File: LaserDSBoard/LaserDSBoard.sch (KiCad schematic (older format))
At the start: 181 parts, among them J1 JTAG, J10 Y LIMIT2, J11 LASER, J12 Y VREF, J13 X VREF, J14 Y1 MOTOR, J15 X MOTOR, J16 Y2 MOTOR, J2 USB, J3 POWER IN, J4 LASER P, J5 D SWITCH, J6 WATER FLOW, J7 X LIMIT1, J8 X LIMIT2, J9 Y LIMIT1, SW1 SW_PUSH, SW2 SWITCH_INV, U1 LD1117S33TR, U10 74HC08A, U11 ADUM1250, U12 TLP2355, U13 TLP2355, U14 TLP2355, U15 TLP2355, U16 TLP2355, U17 TLP2355, U18 74HC1G00, U19 MCP3425, U2 LD1117S33TR, U20 A4982SLPTR, U21 A4982SLPTR, U22 TLP2355, U3 STM32F20XR, U4 LD1117S50TR, U5 ADUM1250, U6 TLP627-4, U7 TLP627, U8 MCP44X1, U9 TLP627, X1 CRYSTAL_4PIN, X2 CRYSTAL

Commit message: DSコントロール基板改版
・2→4層化
・Y軸モータードライバ増設(1→2)
・コネクタ変更
・デジタルポテンショメータ変更
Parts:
- removed C23, C24: 0u1, symbol C_SMALL
- removed D5: X1 Stop, symbol LED
- removed D6: X2 Stop, symbol LED
- removed D7: Y1 Stop, symbol LED
- removed D8: Y2 Stop, symbol LED
- removed J10: Y LIMIT2, ~, symbol CONN2
- removed J3: POWER IN, ~, symbol CONN2
- removed J5: D SWITCH, ~, symbol CONN2
- removed J7: X LIMIT1, ~, symbol CONN2
- removed J8: X LIMIT2, ~, symbol CONN2
- removed J9: Y LIMIT1, ~, symbol CONN2
- removed L1, L2: BLM21SN300SN1D, ~, symbol FILTER
- removed L3: BLM21PG221SN1D, ~, symbol FILTER
- removed R10, R15, R16, R17, R18, R19, R2, R20, R23, R24, R3, R5, R6, R7, R72, R8, R9: 220R, symbol R
- removed R32, R33, R34, R35, R37, R40, R45, R46, R47, R48, R49: 4k7, symbol R
- removed R41, R42, R43, R44, R50: 1k, symbol R
- removed R52: 10k, symbol R_SMALL
- removed R61: 100R, symbol R
- removed TR1: BSH105, ~, symbol BSH105
- removed U1, U2: LD1117S33TR, ~, symbol LD1117S33TR
- removed U10: 74HC08A, ~, symbol 74HC08A
- removed U18: 74HC1G00, ~, symbol 74HC1G00
- removed U6: TLP627-4, ~, symbol TLP627-4
- removed U7, U9: TLP627, ~, symbol TLP627
- removed U8: MCP44X1, symbol MCP44X1
- added C23, C24, C51, C53, C56: 0u1, Capacitors_SMD:C_0805, symbol C-RESCUE-LaserDSBoard
- added C48, C49: 0u1, Capacitors_SMD:C_0805, symbol C_SMALL
- added C50, C54: 0u22, Capacitors_SMD:C_0603, symbol C-RESCUE-LaserDSBoard
- added C52: 100u, Capacitors_SMD:CP_Elec_6.3x7.7, symbol C_POL
- added C55: 0u1, Capacitors_SMD:C_0805, symbol Csmall
- added D5: X1 Stop, Diodes_SMD:D_0603, symbol LED-RESCUE-LaserDSBoard
- added D6: X2 Stop, Diodes_SMD:D_0603, symbol LED-RESCUE-LaserDSBoard
- added D7: Y1 Stop, Diodes_SMD:D_0603, symbol LED-RESCUE-LaserDSBoard
- added D8: Y2 Stop, Diodes_SMD:D_0603, symbol LED-RESCUE-LaserDSBoard
- added J10: D SWITCH, mylib:S3B-XH-SM4-TB, symbol CONN3
- added J17: Y VREF, Pin_Headers:Pin_Header_Straight_1x01_Pitch1.00mm, symbol VREF
- added J3: POWER IN, mylib:VH-4, symbol CONN4
- added J5: X LIMIT1, mylib:S3B-XH-SM4-TB, symbol CONN3
- added J7: X LIMIT2, mylib:S3B-XH-SM4-TB, symbol CONN3
- added J8: Y LIMIT1, mylib:S3B-XH-SM4-TB, symbol CONN3
- added J9: Y LIMIT2, mylib:S3B-XH-SM4-TB, symbol CONN3
- added L1: BNX024H01, mylib:BNX024H01, symbol BNX024H01
- added R10, R15, R16, R17, R18, R19, R20, R23, R24, R32, R9: 1k, Resistors_SMD:R_0603, symbol R-RESCUE-LaserDSBoard
- added R2, R3, R5, R7, R8: 4k7, Resistors_SMD:R_0603, symbol R-RESCUE-LaserDSBoard
- added R33: 10k, Resistors_SMD:R_0603, symbol R-RESCUE-LaserDSBoard
- added R34: 100k, Resistors_SMD:R_0603, symbol R-RESCUE-LaserDSBoard
- added R35, R41: 0R, Resistors_SMD:R_1206, symbol R-RESCUE-LaserDSBoard
- added R37, R40: 0R1, Resistors_SMD:R_1206, symbol R-RESCUE-LaserDSBoard
- added R6: 220R, Resistors_SMD:R_1206, symbol R-RESCUE-LaserDSBoard
- added TP1, TP2, TP3, TP4: CP-10, Pin_Headers:Pin_Header_Straight_1x01_Pitch1.00mm, symbol TEST_1P
- added U1, U2: LD1117S, mylib:LD1117S33TR, symbol LD1117S
- added U10, U18, U6, U7, U8, U9: TLP2355, mylib:TLP2355, symbol TLP2355
- added U23: TPL0401A, TO_SOT_Packages_SMD:SOT-23-6, symbol TPL0401X
- added U24: TPL0401B, TO_SOT_Packages_SMD:SOT-23-6, symbol TPL0401X
- added U25: A4982SLPTR, mylib:A4982SLPTR, symbol A4982SLPTR
- C1, C2, C29, C35, C36, C4, C40, C41, C46, C47, C6, C7, C8: footprint (none) -> Capacitors_SMD:C_0805; symbol C -> C-RESCUE-LaserDSBoard
- C10, C11, C13, C15, C20, C3, C9: footprint (none) -> Capacitors_SMD:C_0603
- C12, C14, C17, C18, C19, C21, C22, C25, C26, C27, C28, C30, C31, C33, C39: footprint (none) -> Capacitors_SMD:C_0805
- C16: footprint ~ -> Capacitors_SMD:C_0805; symbol CP1 -> CP1-RESCUE-LaserDSBoard
- C32, C34, C42, C43: footprint (none) -> Capacitors_SMD:C_0603; symbol C -> C-RESCUE-LaserDSBoard
- C37, C38, C5: footprint (none) -> Capacitors_SMD:CP_Elec_6.3x7.7
- C44, C45: footprint (none) -> Capacitors_SMD:C_0805; symbol CSMALL -> Csmall
- D1, D2, D3, D4, D9: footprint (none) -> Diodes_SMD:D_0603; symbol LED -> LED-RESCUE-LaserDSBoard
- J1: footprint (none) -> Pin_Headers:Pin_Header_Straight_2x05_Pitch1.00mm
- J11, J4, J6: footprint ~ -> mylib:S3B-XH-SM4-TB
- J12, J13: footprint (none) -> Pin_Headers:Pin_Header_Straight_1x01_Pitch1.00mm
- J14, J15, J16: footprint ~ -> mylib:VH-4
- J2: footprint ~ -> mylib:USB_B
- L4: value Ferrite bead -> LI0603G221R-10; footprint ~ -> Resistors_SMD:R_0603
- R1, R11, R12, R13, R14, R21, R22, R29, R30, R31, R39, R53, R54, R62, R63: footprint (none) -> Resistors_SMD:R_0603
- R25, R26, R27, R64, R67, R68, R69: footprint (none) -> Resistors_SMD:R_0603; symbol R -> R-RESCUE-LaserDSBoard
- R28, R4, R51, R55, R56, R57, R58, R59, R60, R65, R70, R71, R73, R74, R75, R76: footprint (none) -> Resistors_SMD:R_1206; symbol R -> R-RESCUE-LaserDSBoard
- R36, R38: value 4k7 -> 1k; footprint (none) -> Resistors_SMD:R_0603
- R66: footprint 0603 -> Resistors_SMD:R_0603; symbol R -> R-RESCUE-LaserDSBoard
- SW1: value SW_PUSH -> DHT-1163S; footprint ~ -> mylib:DHT-1163S
- SW2: value SWITCH_INV -> SSSS213202; footprint ~ -> mylib:SSSS213202
- U11, U5: footprint (none) -> mylib:ADUM1250
- U12, U13, U14, U15, U16, U17, U22: footprint ~ -> mylib:TLP2355
- U19: footprint ~ -> mylib:MCP3425
- U20: footprint ~ -> mylib:A4982SLPTR
- U21: footprint (none) -> mylib:A4982SLPTR
- U3: footprint LQFP64 -> Housings_QFP:LQFP-64_10x10mm_Pitch0.5mm
- U4: value LD1117S50TR -> LD1117S; footprint ~ -> mylib:LD1117S33TR
- VR1, VR2: footprint ~ -> Capacitors_SMD:C_0603
- X1: value CRYSTAL_4PIN -> 7B-25.000MAAJ-T; footprint ~ -> Oscillators:Oscillator_SMD_Fordahl_DFAS15-4pin_5.0x3.2mm
- X2: value CRYSTAL -> 9HT10-32.768KDZY-T; footprint ~ -> Capacitors_SMD:C_1206; symbol CRYSTAL -> CRYSTAL-RESCUE-LaserDSBoard
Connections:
- net labels added: +12P, +12VA, +3V3, +5VA, A+12V, A+3.3V, A+5V, D+3.3V, GNDA, GNDD, GNDPWR, Y1_MOT_1A, Y1_MOT_1B, Y1_MOT_2A, Y1_MOT_2B, Y2_MOT_1A, Y2_MOT_1B, Y2_MOT_2A, Y2_MOT_2B, Y_DIR_A, Y_EN_A, Y_STEP_A
- net labels removed: +3.3V, D12V, D33V, D5V, DGND, GND, Y_MOT_1A, Y_MOT_1B, Y_MOT_2A, Y_MOT_2B
- wire segments 666 -> 687
- no-connect marks 35 -> 25
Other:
- note added: "12V Voltage Monitor"
- note added: "Common GND"
- note added: "GND PIN"
- note added: "Limit switch IF\nD switch IF\nWATER FLOW IF\n"
- note added: "POWER ANALOG"
- note added: "POWER DIGITAL"
- note removed: "12V Input"
- moved on the sheet: C1, C11, C12, C13, C14, C15, C16, C17, C18, C19, C2, C20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

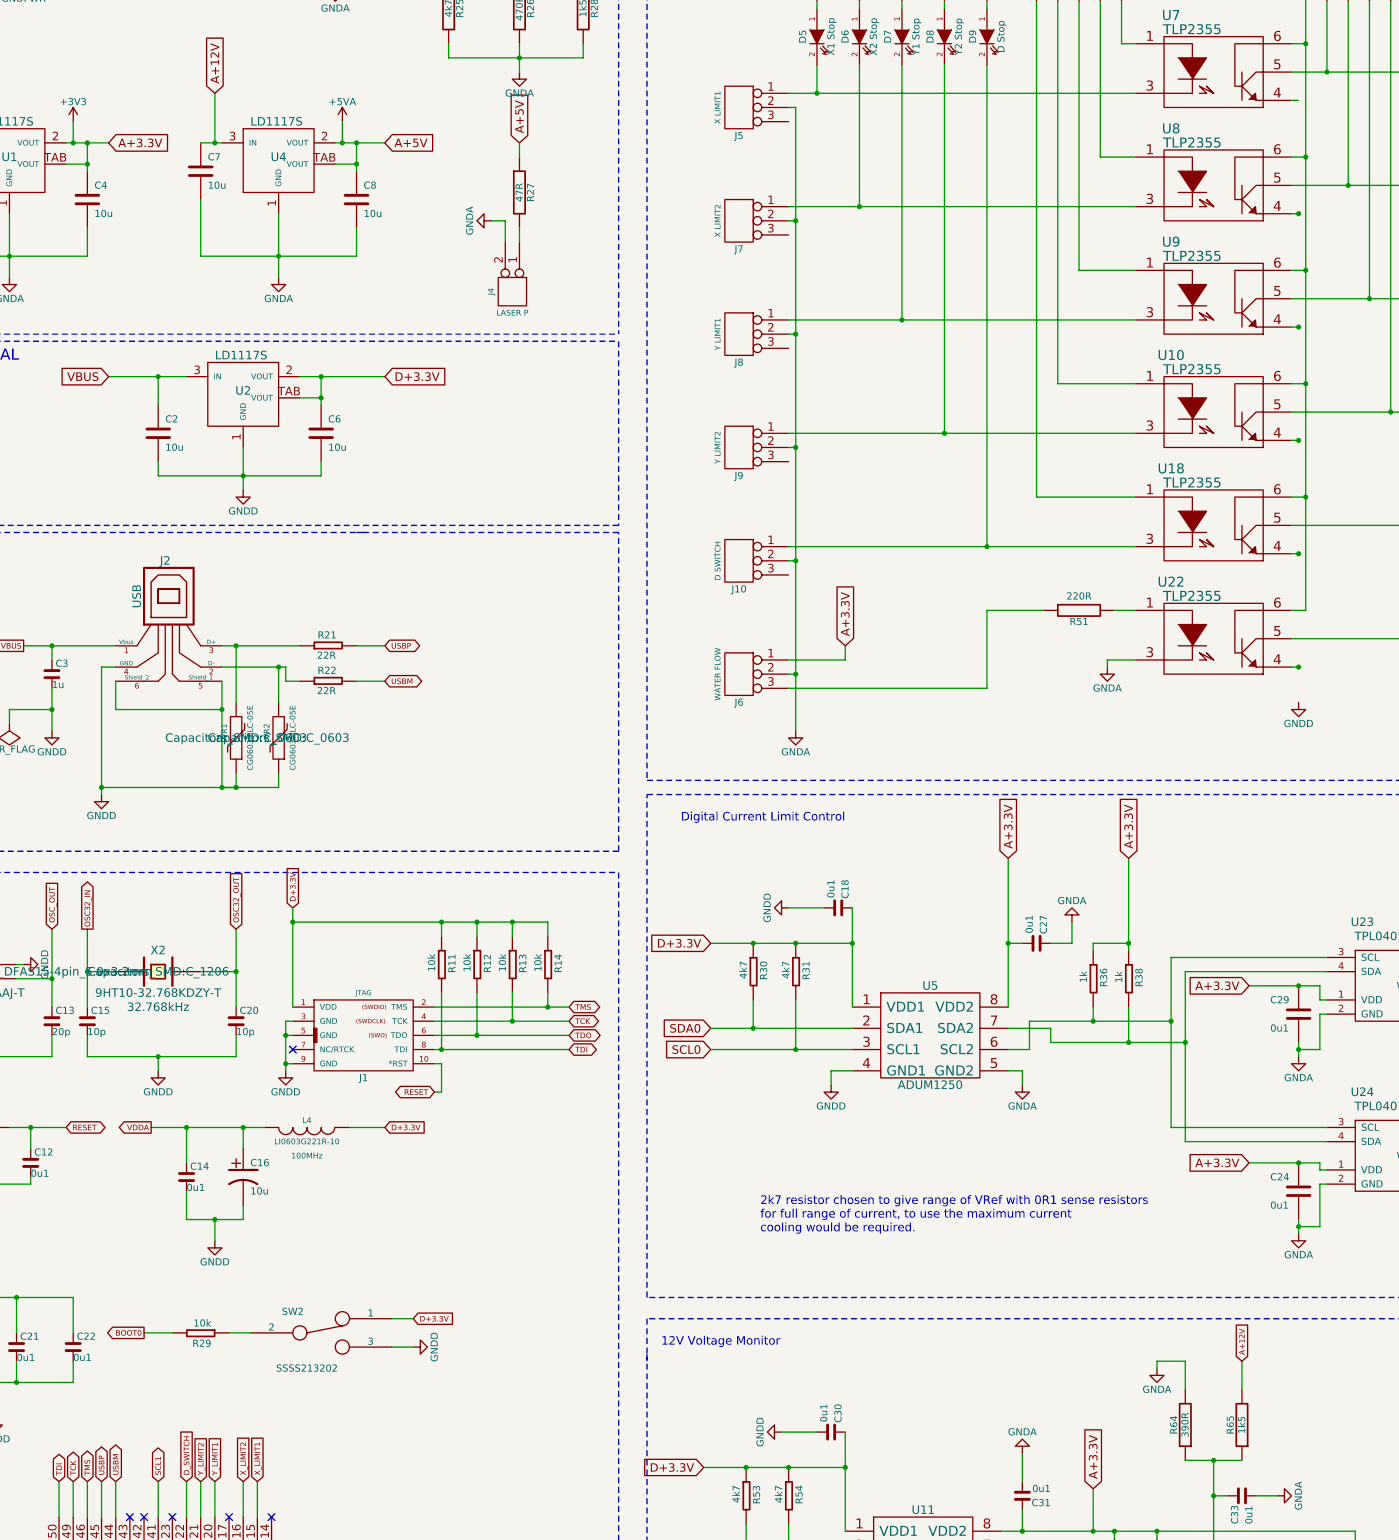
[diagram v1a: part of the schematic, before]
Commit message: ver 2.0
- DFUモード用のLEDを追加
-フォトカプラ改修(GND接続)
- R28 R4 R65 パッドサイズを0603に変更
- 部品表 1k パッドサイズ1206→0603
-TPL0401 PADピッチ誤り修正（TO-SOT23-6→カスタムPAD）
-TP穴径変更
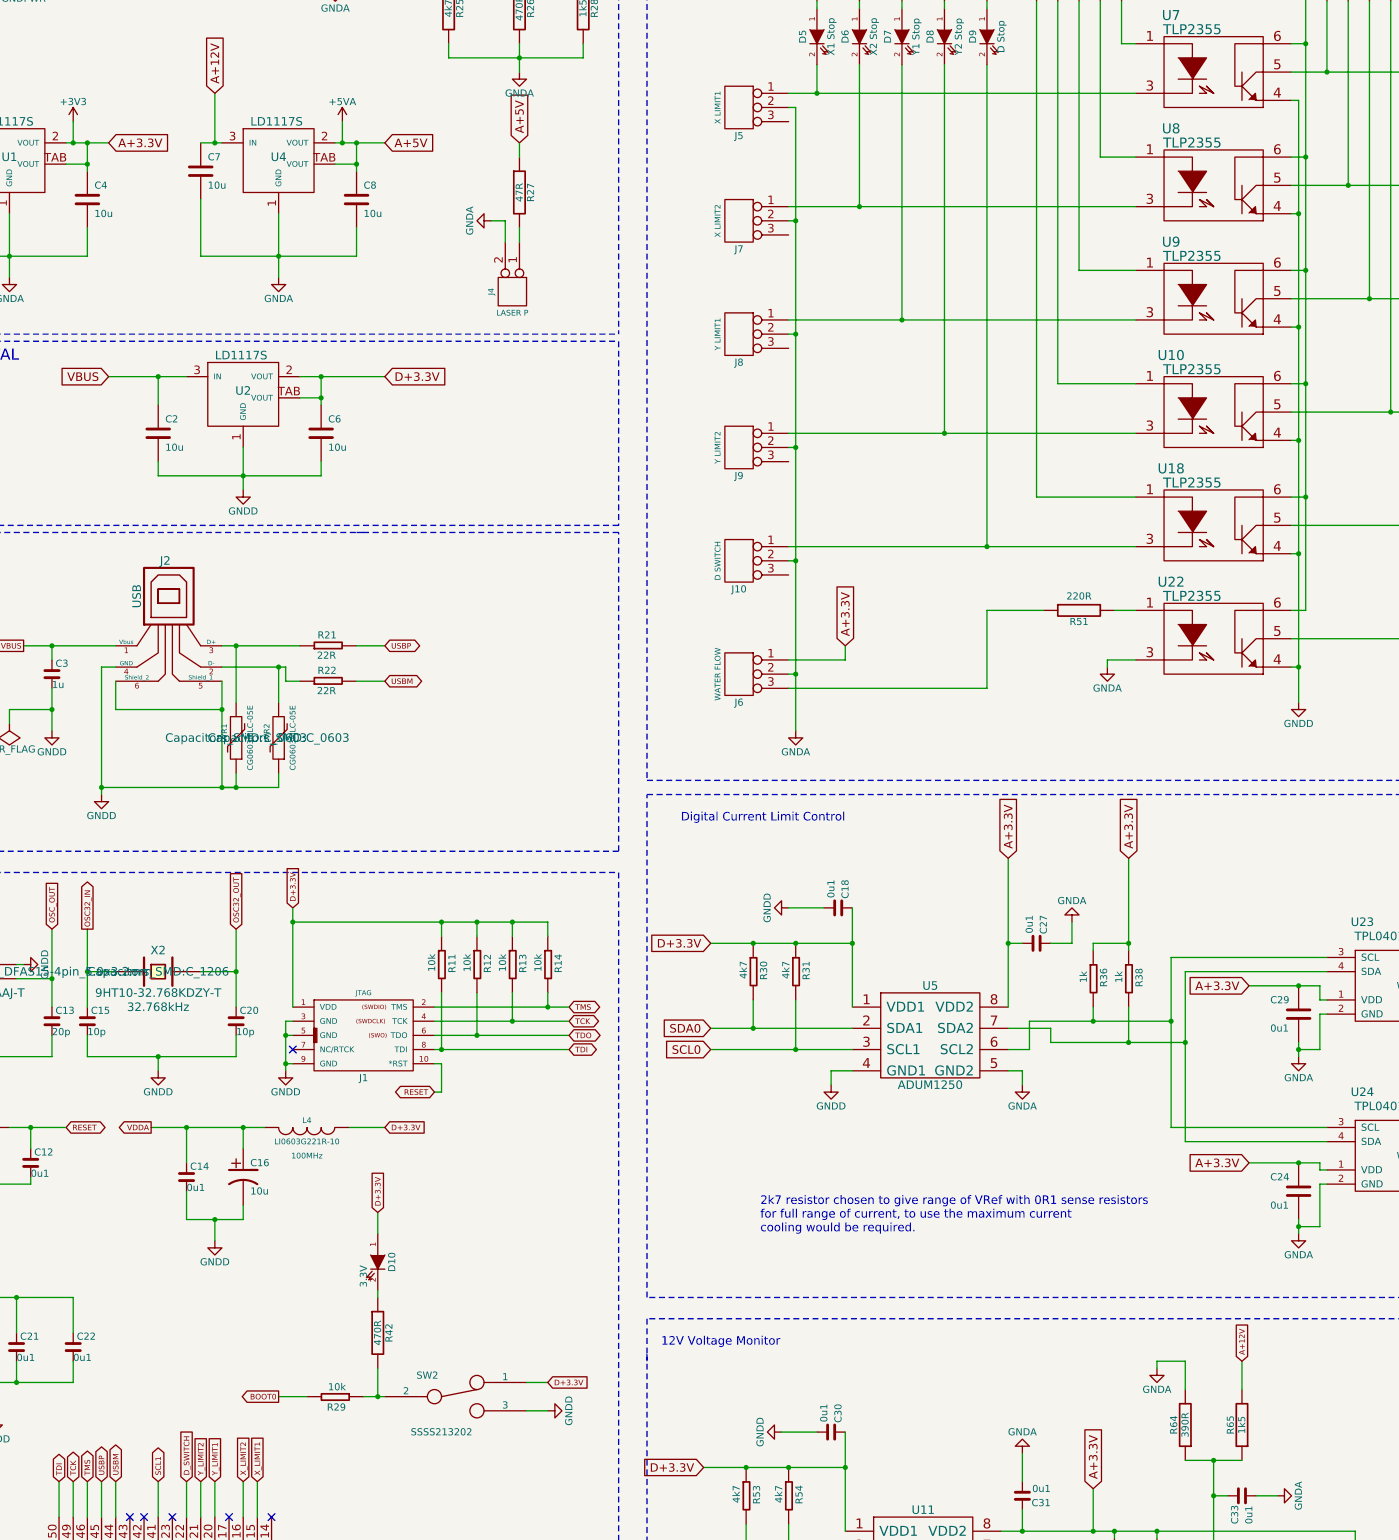
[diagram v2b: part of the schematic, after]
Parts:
- added D10: 3.3V, Diodes_SMD:D_0603, symbol LED-RESCUE-LaserDSBoard
- added R42: 470R, Resistors_SMD:R_0603, symbol R-RESCUE-LaserDSBoard
- R28, R4, R65: footprint Resistors_SMD:R_1206 -> Resistors_SMD:R_0603
- TP1, TP2, TP3, TP4: footprint Pin_Headers:Pin_Header_Straight_1x01_Pitch1.00mm -> Pin_Headers:Pin_Header_Straight_1x01_Pitch2.54mm
- U23, U24: footprint TO_SOT_Packages_SMD:SOT-23-6 -> mylib:TPL0401
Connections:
- net D+3.3V: now also D10.1 (A)
- net GNDD: now also U10.4, U18.4, U22.4, U7.4, U8.4, U9.4
- net at R29.1, SW2.2: now also R42.2
- new net: D10.2 (K), R42.1
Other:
- moved on the sheet: R29, SW2
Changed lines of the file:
@@
 Sheet 1 1
 Title "LaserDSBoard"
-Date "21 dec 2017"
-Rev "1.0.0"
+Date "2018-04-10"
+Rev "2.0.0"
 Comp "smartDIYs Co.,Ltd."
 Comment1 "http://www.smartdiys.com/"
@@
 F 0 "R28" V 5580 1800 50  0000 C CNN
 F 1 "1k5" V 5500 1800 50  0000 C CNN
-F 2 "Resistors_SMD:R_1206" H 5500 1800 60  0001 C CNN
+F 2 "Resistors_SMD:R_0603" H 5500 1800 60  0001 C CNN
 F 3 "" H 5500 1800 60  0001 C CNN
 	1    5500 1800
@@
 L R_SMALL R29
 U 1 1 56CF0F9B
-P 2800 11150
-F 0 "R29" V 2875 11158 50  0000 C CNN
-F 1 "10k" V 2732 11162 50  0000 C CNN
-F 2 "Resistors_SMD:R_0603" H 2800 11150 60  0001 C CNN
-F 3 "" H 2800 11150 60  0001 C CNN
-	1    2800 11150
+P 3750 11600
+F 0 "R29" V 3825 11608 50  0000 C CNN
+F 1 "10k" V 3682 11612 50  0000 C CNN
+F 2 "Resistors_SMD:R_0603" H 3750 11600 60  0001 C CNN
+F 3 "" H 3750 11600 60  0001 C CNN
+	1    3750 11600
 	0    1    1    0
 $EndComp
@@
 F 0 "R4" V 1030 7000 50  0000 C CNN
 F 1 "1k5" V 950 7000 50  0000 C CNN
-F 2 "Resistors_SMD:R_1206" H 950 7000 60  0001 C CNN
+F 2 "Resistors_SMD:R_0603" H 950 7000 60  0001 C CNN
 F 3 "" H 950 7000 60  0001 C CNN
 	1    950  7000
@@
 	-1   0    0    1
 $EndComp
-Text GLabel 4300 11050 2    39   Input ~ 0
+Text GLabel 5250 11500 2    39   Input ~ 0
 D+3.3V
 $Comp
 L SWITCH_INV SW2
 U 1 1 5726C615
-P 3650 11150
-F 0 "SW2" H 3450 11300 50  0000 C CNN
-F 1 "SSSS213202" H 3550 10900 50  0000 C CNN
-F 2 "mylib:SSSS213202" H 3650 11150 60  0001 C CNN
-F 3 "~" H 3650 11150 60  0000 C CNN
-	1    3650 11150
+P 4600 11600
+F 0 "SW2" H 4400 11750 50  0000 C CNN
+F 1 "SSSS213202" H 4500 11350 50  0000 C CNN
+F 2 "mylib:SSSS213202" H 4600 11600 60  0001 C CNN
+F 3 "~" H 4600 11600 60  0000 C CNN
+	1    4600 11600
 	1    0    0    -1
 $EndComp
 Text GLabel 4400 13550 2    39   Input ~ 0
 BOOT0
-Text GLabel 2400 11150 0    39   Output ~ 0
+Text GLabel 3350 11600 0    39   Output ~ 0
 BOOT0
 $Comp
@@
 F 0 "R65" V 10230 11800 50  0000 C CNN
 F 1 "1k5" V 10150 11800 50  0000 C CNN
-F 2 "Resistors_SMD:R_1206" H 10150 11800 60  0001 C CNN
+F 2 "Resistors_SMD:R_0603" H 10150 11800 60  0001 C CNN
 F 3 "" H 10150 11800 60  0001 C CNN
 	1    10150 11800
@@
 F 0 "U23" H 11000 8950 60  0000 C CNN
 F 1 "TPL0401A" H 11150 8850 60  0000 C CNN
-F 2 "TO_SOT_Packages_SMD:SOT-23-6" H 11200 8600 60  0001 C CNN
+F 2 "mylib:TPL0401" H 11200 8600 60  0001 C CNN
 F 3 "" H 11200 8600 60  0000 C CNN
 	1    11200 8600
@@
 F 0 "U24" H 11000 10150 60  0000 C CNN
 F 1 "TPL0401B" H 11150 10050 60  0000 C CNN
-F 2 "TO_SOT_Packages_SMD:SOT-23-6" H 11200 9800 60  0001 C CNN
+F 2 "mylib:TPL0401" H 11200 9800 60  0001 C CNN
 F 3 "" H 11200 9800 60  0000 C CNN
 	1    11200 9800
@@
 L GNDD #PWR025
 U 1 1 5A872F81
-P 4300 11250
-F 0 "#PWR025" H 4300 11000 50  0001 C CNN
-F 1 "GNDD" H 4300 11100 50  0000 C CNN
-F 2 "" H 4300 11250 50  0000 C CNN
-F 3 "" H 4300 11250 50  0000 C CNN
-	1    4300 11250
+P 5250 11700
+F 0 "#PWR025" H 5250 11450 50  0001 C CNN
+F 1 "GNDD" H 5250 11550 50  0000 C CNN
+F 2 "" H 5250 11700 50  0000 C CNN
+F 3 "" H 5250 11700 50  0000 C CNN
+	1    5250 11700
 	0    -1   -1   0
 $EndComp
@@
 	800  13600 1300 13600
 Wire Wire Line
-	4150 11050 4300 11050
+	5100 11500 5250 11500
 Wire Wire Line
-	4150 11250 4300 11250
+	5100 11700 5250 11700
 Wire Wire Line
-	3000 11150 3150 11150
+	3950 11600 4100 11600
 Wire Wire Line
-	2600 11150 2400 11150
+	3550 11600 3350 11600
 Wire Wire Line
 	3050 6700 3050 6300
@@
 F 0 "TP1" H 13650 15070 50  0000 C CNN
 F 1 "CP-10" H 13650 15000 50  0000 C CNN
-F 2 "Pin_Headers:Pin_Header_Straight_1x01_Pitch1.00mm" H 13850 14800 50  0001 C CNN
+F 2 "Pin_Headers:Pin_Header_Straight_1x01_Pitch2.54mm" H 13850 14800 50  0001 C CNN
 F 3 "" H 13850 14800 50  0000 C CNN
 	1    13650 14800
@@
 F 0 "TP2" H 14000 15070 50  0000 C CNN
 F 1 "CP-10" H 14000 15000 50  0000 C CNN
-F 2 "Pin_Headers:Pin_Header_Straight_1x01_Pitch1.00mm" H 14200 14800 50  0001 C CNN
+F 2 "Pin_Headers:Pin_Header_Straight_1x01_Pitch2.54mm" H 14200 14800 50  0001 C CNN
 F 3 "" H 14200 14800 50  0000 C CNN
 	1    14000 14800
@@
 F 0 "TP3" H 14350 15070 50  0000 C CNN
 F 1 "CP-10" H 14350 15000 50  0000 C CNN
-F 2 "Pin_Headers:Pin_Header_Straight_1x01_Pitch1.00mm" H 14550 14800 50  0001 C CNN
+F 2 "Pin_Headers:Pin_Header_Straight_1x01_Pitch2.54mm" H 14550 14800 50  0001 C CNN
 F 3 "" H 14550 14800 50  0000 C CNN
 	1    14350 14800
@@
 F 0 "TP4" H 14750 15070 50  0000 C CNN
 F 1 "CP-10" H 14750 15000 50  0000 C CNN
-F 2 "Pin_Headers:Pin_Header_Straight_1x01_Pitch1.00mm" H 14950 14800 50  0001 C CNN
+F 2 "Pin_Headers:Pin_Header_Straight_1x01_Pitch2.54mm" H 14950 14800 50  0001 C CNN
 F 3 "" H 14950 14800 50  0000 C CNN
 	1    14750 14800
@@
 Wire Wire Line
 	10500 3650 10600 3650
+$Comp
+L R-RESCUE-LaserDSBoard R42
+U 1 1 5AC57081
+P 4050 11150
+F 0 "R42" V 4130 11150 50  0000 C CNN
+F 1 "470R" V 4050 11150 50  0000 C CNN
+F 2 "Resistors_SMD:R_0603" H 4050 11150 60  0001 C CNN
+F 3 "" H 4050 11150 60  0001 C CNN
+	1    4050 11150
+	1    0    0    -1
+$EndComp
+$Comp
+L LED-RESCUE-LaserDSBoard D10
+U 1 1 5AC57087
+P 4050 10650
+F 0 "D10" H 4050 10750 50  0000 C CNN
+F 1 "3.3V" H 4150 10550 50  0000 C CNN
+F 2 "Diodes_SMD:D_0603" H 4050 10650 60  0001 C CNN
+F 3 "" H 4050 10650 60  0001 C CNN
+	1    4050 10650
+	0    1    1    0
+$EndComp
+Wire Wire Line
+	4050 10300 4050 10450
+Wire Wire Line
+	4050 10900 4050 10850
+Wire Wire Line
+	4050 11400 4050 11600
+Connection ~ 4050 11600
+Wire Wire Line
+	10550 2450 10550 6700
+Text GLabel 4050 10300 1    39   Input ~ 0
+D+3.3V
 $EndSCHEMATC
